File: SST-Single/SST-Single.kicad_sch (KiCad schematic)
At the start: 13 parts, among them J1 MJ-179PH, J2 Conn_01x03_Pin, J3 Conn_01x04_Pin, Q1 2SJ498-D, U1 FT231XS_Breakout, U2 LT1785AxN8

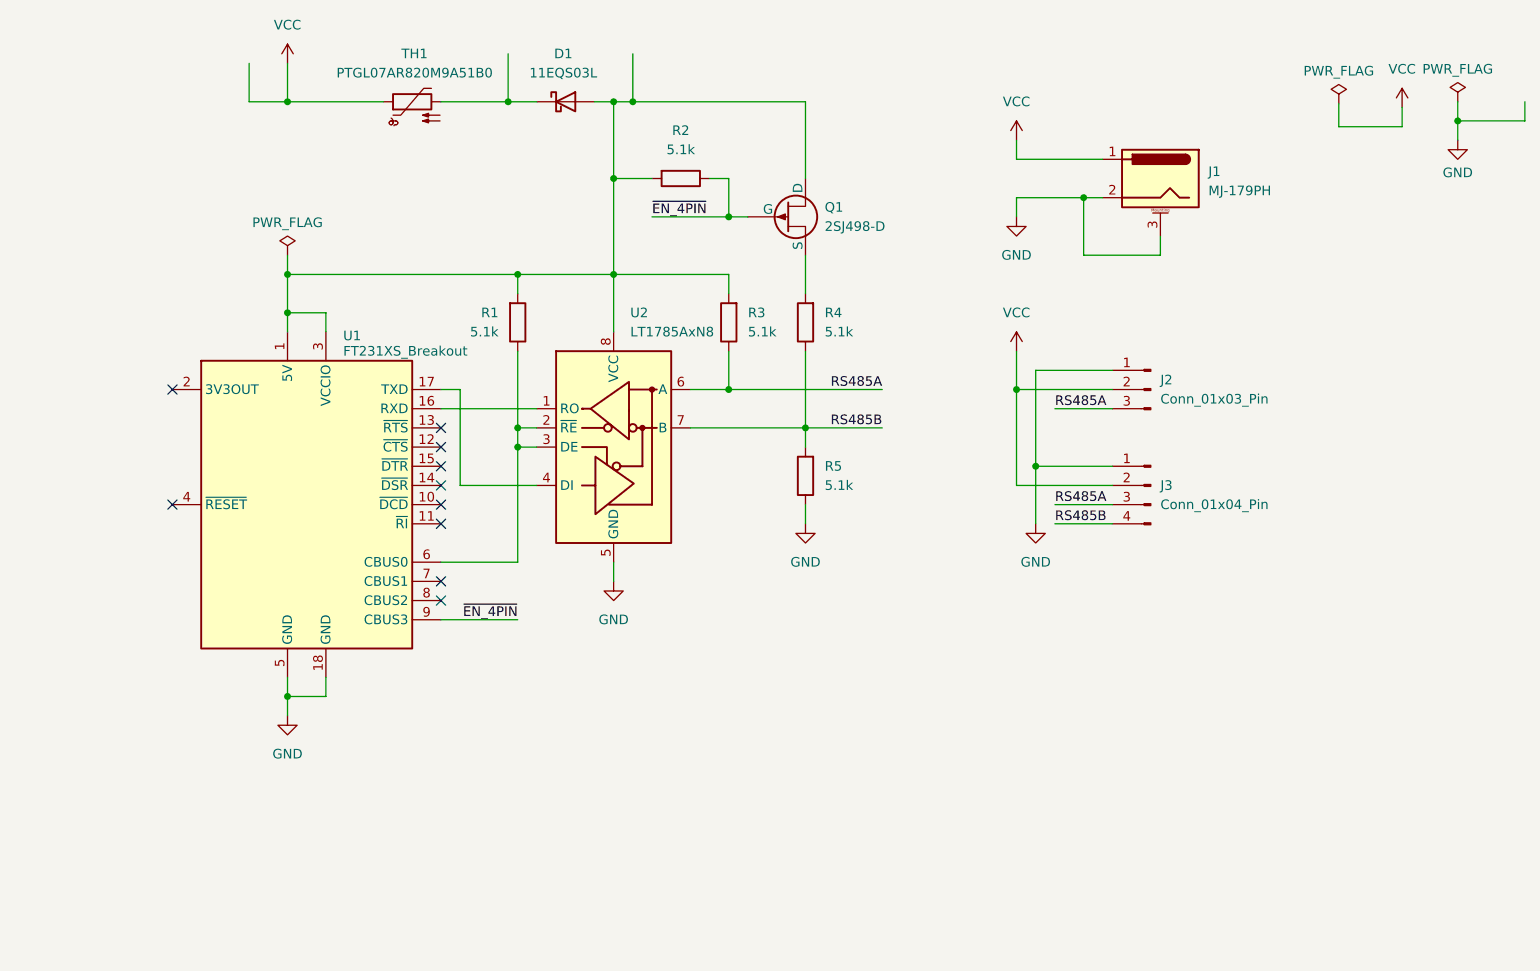
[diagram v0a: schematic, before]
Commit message: Add DIP switch to select serial mode
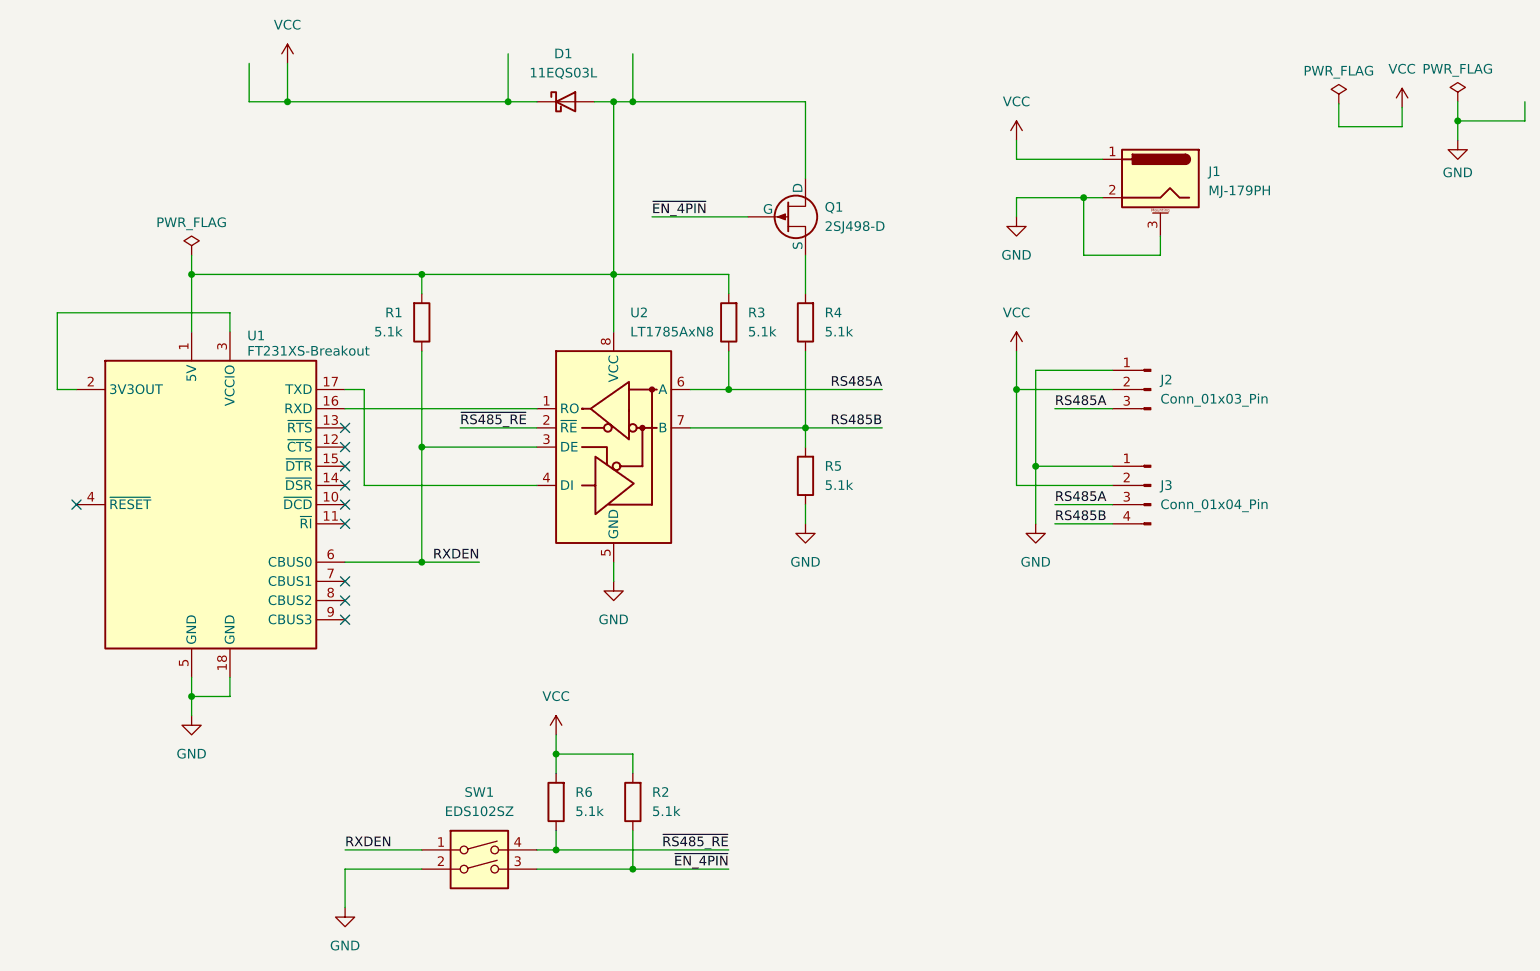
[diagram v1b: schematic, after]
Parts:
- removed TH1: PTGL07AR820M9A51B0, Capacitor_THT:C_Disc_D8.0mm_W5.0mm_P5.00mm, symbol Device:Thermistor_PTC
- added R6: 5.1k, Resistor_THT:R_Axial_DIN0207_L6.3mm_D2.5mm_P10.16mm_Horizontal, symbol Device:R
- added SW1: EDS102SZ, Button_Switch_THT:SW_DIP_SPSTx02_Slide_9.78x7.26mm_W7.62mm_P2.54mm, symbol Switch:SW_DIP_x02
- U1: value FT231XS_Breakout -> FT231XS-Breakout
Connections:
- net GND: now also SW1.2
- net VCC: now also D1.1 (K), R2.2, R6.2
- net ~{EN_4PIN}: now also SW1.3; no longer U1.9 (CBUS3)
- net at D1.2 (A), Q1.1 (D), R1.2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: no longer R2.2, U1.3 (VCCIO)
- net RXDEN: now reaches R1.1, U1.6 (CBUS0), U2.3 (DE)
- net RXDEN: now also SW1.1; no longer U2.2 (~{RE})
- net at U1.2 (3V3OUT): now also U1.3 (VCCIO)
- new net ~{RS485_RE}: R6.1, SW1.4, U2.2 (~{RE})
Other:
- moved on the sheet: R1, U1

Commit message: Remove FET and modify resistors of RS485 DE line
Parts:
- removed Q1: 2SJ498-D, Package_TO_SOT_THT:TO-92S_Wide, symbol Simulation_SPICE:PJFET
- removed R2, R6: 5.1k, Resistor_THT:R_Axial_DIN0207_L6.3mm_D2.5mm_P10.16mm_Horizontal, symbol Device:R
- added D2: OSR6LU5B64A-12V, LED_THT:LED_D5.0mm, symbol Device:LED
- added H1, H2, H3, H4: MountingHole, MountingHole:MountingHole_3.2mm_M3, symbol Mechanical:MountingHole
- renumbered J2 to J1, J3 to J2, J1 to J3, R3 to R2, R4 to R3, R5 to R4
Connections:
- net ~{EN_4PIN} is gone; now on net ~{RS485_RE}: SW1.3
- net GND: now also R1.1, D2.1 (K); no longer SW1.2
- net RXDEN: now also SW1.2; no longer R1.1, SW1.1
- net ~{RS485_RE}: now also R1.2; no longer SW1.4
- net RS485B_UP: now reaches R3.2
- net RS485B_UP: now also SW1.4
- net +5V: now reaches D1.2 (A), R2.2, U1.1 (5V), U2.8 (VCC)
- net +5V: now also SW1.1, D2.2 (A); no longer R1.2
- net RXD: now reaches U1.16 (RXD), U2.1 (RO)
- net TXD: now reaches U1.17 (TXD), U2.4 (DI)
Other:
- moved on the sheet: D1, R2, R3, R4, SW1, U2
